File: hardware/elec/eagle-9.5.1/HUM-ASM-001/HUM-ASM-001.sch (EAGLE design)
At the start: 63 parts, among them J2 75869-131LF, J20 75869-131LF, J21 75869-131LF, J3 B2B-XH-AM(LF)(SN), K1 7-1393239-7, K2 7-1393239-7, Q1 IRLB8721PBF, Q2 IRLB8721PBF, U1 MCP23017-E/SP

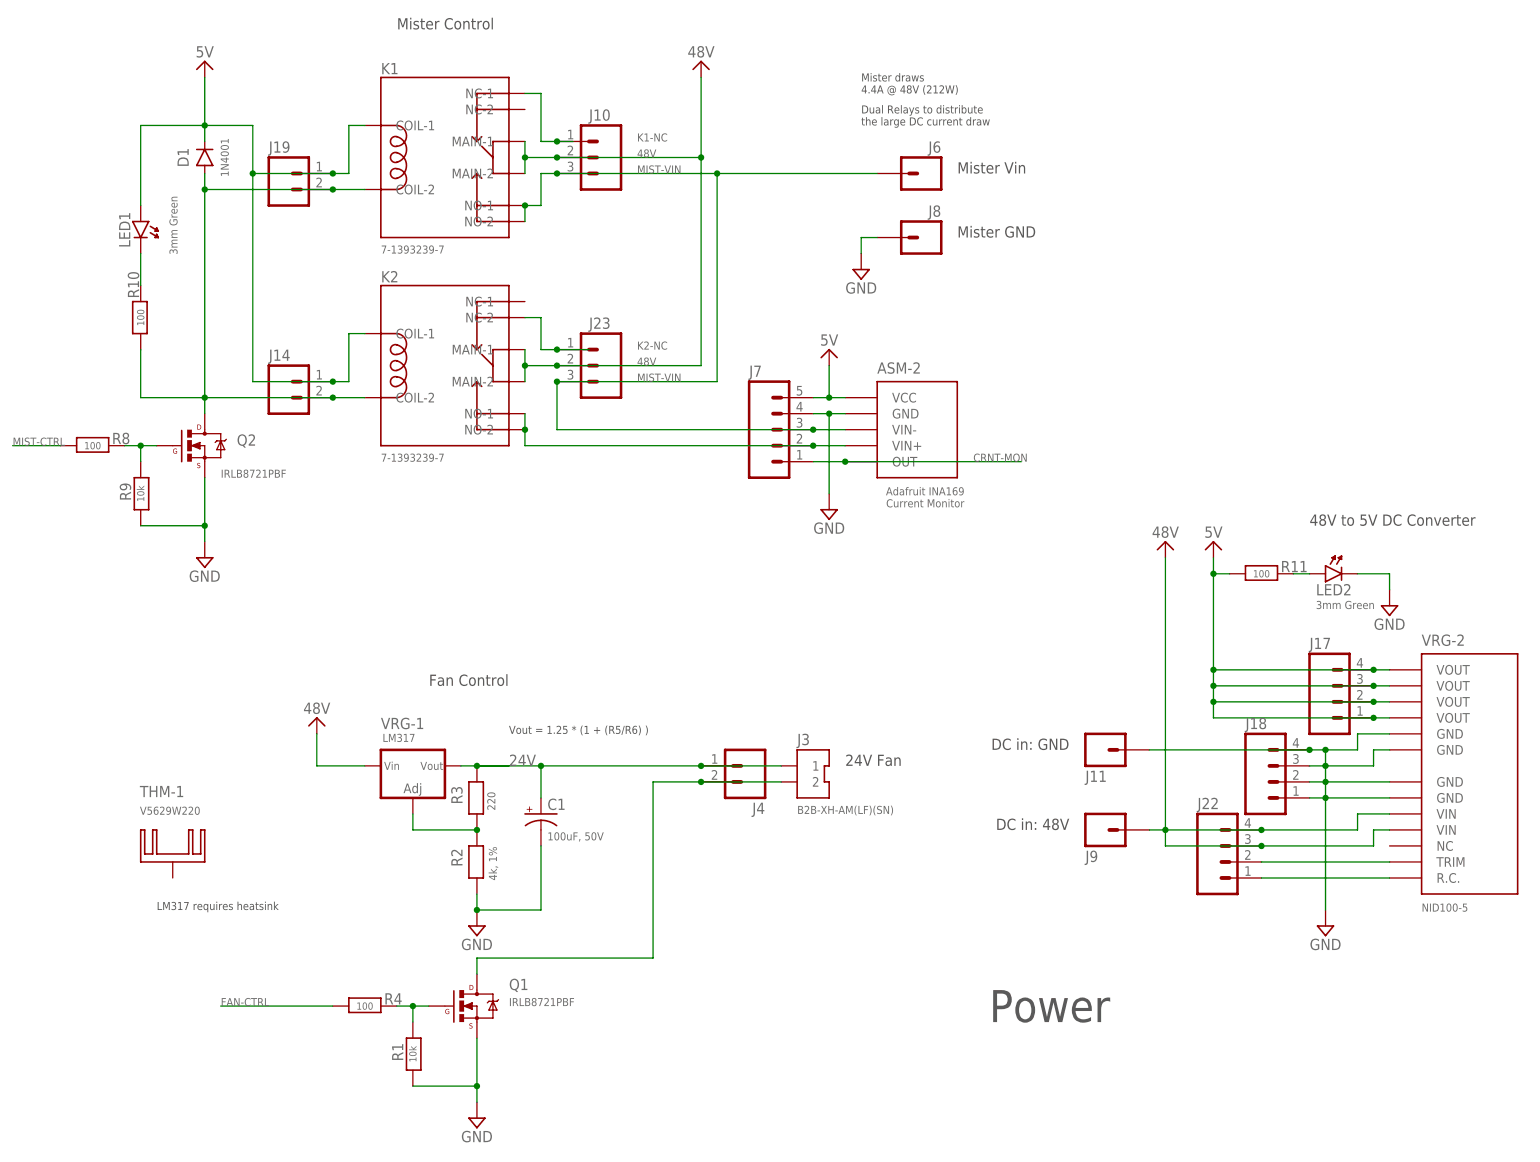
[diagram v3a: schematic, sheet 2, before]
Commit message: * Final PCB v1.0 edits * Exported Gerber files and send to fab
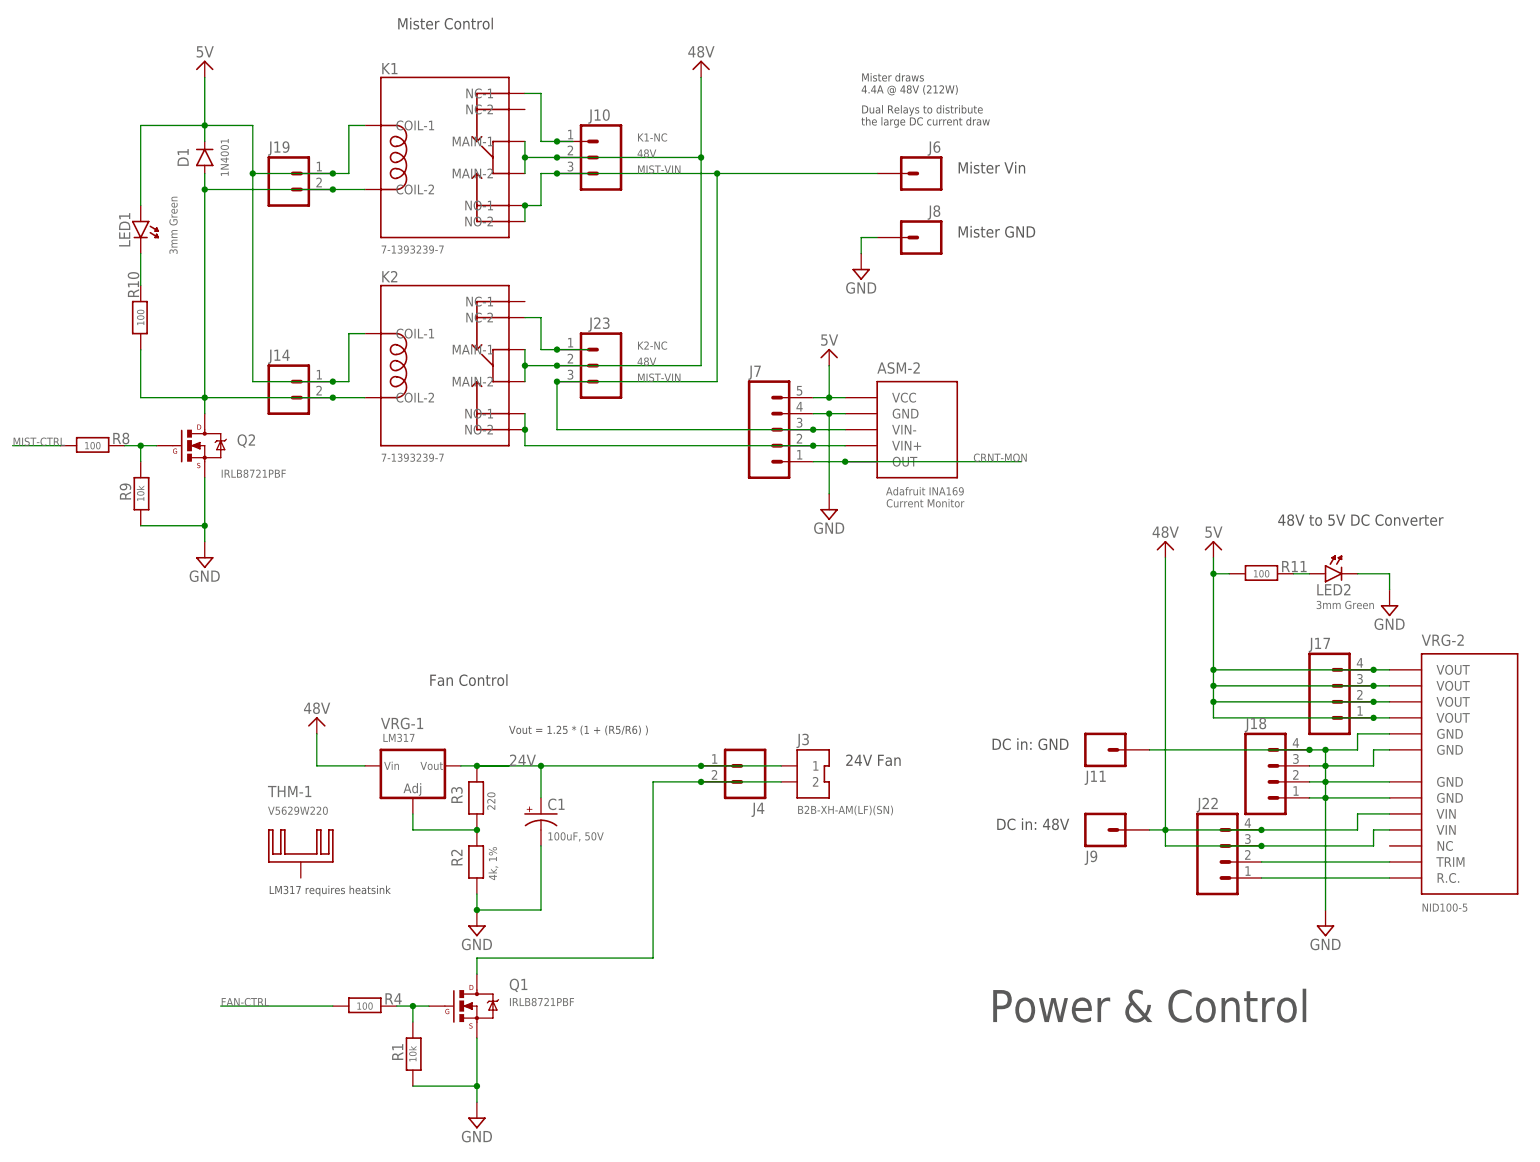
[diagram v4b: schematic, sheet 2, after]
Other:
- note added: "Power & Control"
- note removed: "Power"
- moved on the sheet: THM-1
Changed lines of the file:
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@@
 <description>Power</description>
 <plain>
-<text x="165.1" y="-170.18" size="5.08" layer="97" font="vector">Power</text>
+<text x="165.1" y="-170.18" size="5.08" layer="97" font="vector">Power &amp; Control</text>
 <text x="144.78" y="-22.86" size="1.27" layer="97" font="vector">Mister draws
 4.4A @ 48V (212W)</text>
 <text x="144.78" y="-27.94" size="1.27" layer="97" font="vector">Dual Relays to distribute
 the large DC current draw</text>
-<text x="215.9" y="-91.44" size="1.778" layer="97" font="vector">48V to 5V DC Converter</text>
+<text x="210.82" y="-91.44" size="1.778" layer="97" font="vector">48V to 5V DC Converter</text>
 <text x="71.12" y="-12.7" size="1.778" layer="97" font="vector">Mister Control</text>
 <text x="88.9" y="-124.46" size="1.27" layer="97" font="vector">Vout = 1.25 * (1 + (R5/R6) )</text>
 <text x="142.24" y="-129.54" size="1.778" layer="97" font="vector">24V Fan</text>
-<text x="33.02" y="-152.4" size="1.27" layer="97" font="vector">LM317 requires heatsink</text>
+<text x="50.8" y="-149.86" size="1.27" layer="97" font="vector">LM317 requires heatsink</text>
 <text x="76.2" y="-116.84" size="1.778" layer="97" font="vector">Fan Control</text>
 <text x="177.8" y="-127" size="1.778" layer="97" font="vector" rot="MR0">DC in: GND</text>
@@
 <attribute name="VALUE" x="88.9" y="-167.64" size="1.27" layer="96" font="vector"/>
 </instance>
-<instance part="THM-1" gate="G$1" x="35.56" y="-144.78" smashed="yes">
-<attribute name="NAME" x="30.353" y="-134.493" size="1.778" layer="95"/>
-<attribute name="VALUE" x="30.353" y="-137.287" size="1.27" layer="96"/>
+<instance part="THM-1" gate="G$1" x="55.88" y="-144.78" smashed="yes">
+<attribute name="NAME" x="50.673" y="-134.493" size="1.778" layer="95"/>
+<attribute name="VALUE" x="50.673" y="-137.287" size="1.27" layer="96"/>
 </instance>
 <instance part="J3" gate="G$1" x="137.16" y="-132.08" smashed="yes">
